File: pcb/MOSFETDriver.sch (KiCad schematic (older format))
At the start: 3 parts

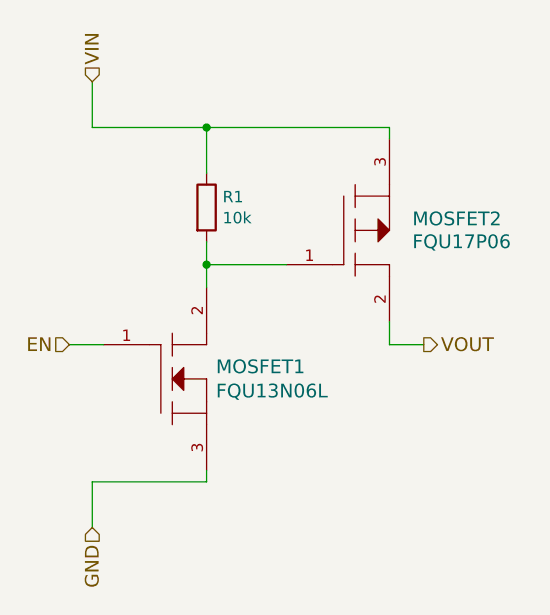
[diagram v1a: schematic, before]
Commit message: Display board connects via 6-wire connector
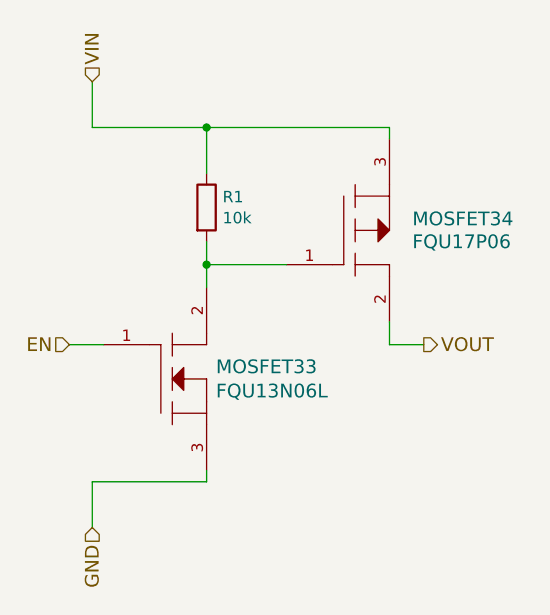
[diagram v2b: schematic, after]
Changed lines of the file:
@@
 $Descr A4 11693 8268
 encoding utf-8
-Sheet 2 19
+Sheet 19 19
 Title "Failinator"
 Date ""
@@
 AR Path="/56946533/56877F77" Ref="MOSFET45"  Part="1"
 AR Path="/5694653F/56877F77" Ref="MOSFET47"  Part="1"
-F 0 "MOSFET1" H 4991 4103 60  0000 L CNN
+AR Path="/5694859C/56932920/56877F77" Ref="MOSFET11"  Part="1"
+AR Path="/5694859C/56930DD4/56877F77" Ref="MOSFET7"  Part="1"
+AR Path="/5694859C/56931957/56877F77" Ref="MOSFET9"  Part="1"
+AR Path="/5694859C/56932F11/56877F77" Ref="MOSFET13"  Part="1"
+AR Path="/5694859C/5693327A/56877F77" Ref="MOSFET15"  Part="1"
+AR Path="/5694859C/56933823/56877F77" Ref="MOSFET17"  Part="1"
+AR Path="/5694859C/5693448C/56877F77" Ref="MOSFET19"  Part="1"
+AR Path="/5694859C/569464F7/56877F77" Ref="MOSFET21"  Part="1"
+AR Path="/5694859C/56946503/56877F77" Ref="MOSFET23"  Part="1"
+AR Path="/5694859C/5694650F/56877F77" Ref="MOSFET25"  Part="1"
+AR Path="/5694859C/5694651B/56877F77" Ref="MOSFET27"  Part="1"
+AR Path="/5694859C/56946527/56877F77" Ref="MOSFET29"  Part="1"
+AR Path="/5694859C/56946533/56877F77" Ref="MOSFET31"  Part="1"
+AR Path="/5694859C/5694653F/56877F77" Ref="MOSFET33"  Part="1"
+F 0 "MOSFET33" H 4991 4103 60  0000 L CNN
 F 1 "FQU13N06L" H 4991 3997 60  0000 L CNN
 F 2 "failinator:TO-251AA" H 4650 4050 60  0001 C CNN
@@
 AR Path="/56946533/56877F80" Ref="R16"  Part="1"
 AR Path="/5694653F/56877F80" Ref="R17"  Part="1"
+AR Path="/5694859C/56932920/56877F80" Ref="R1"  Part="1"
+AR Path="/5694859C/56930DD4/56877F80" Ref="R1"  Part="1"
+AR Path="/5694859C/56931957/56877F80" Ref="R1"  Part="1"
+AR Path="/5694859C/56932F11/56877F80" Ref="R1"  Part="1"
+AR Path="/5694859C/5693327A/56877F80" Ref="R1"  Part="1"
+AR Path="/5694859C/56933823/56877F80" Ref="R1"  Part="1"
+AR Path="/5694859C/5693448C/56877F80" Ref="R1"  Part="1"
+AR Path="/5694859C/569464F7/56877F80" Ref="R1"  Part="1"
+AR Path="/5694859C/56946503/56877F80" Ref="R1"  Part="1"
+AR Path="/5694859C/5694650F/56877F80" Ref="R1"  Part="1"
+AR Path="/5694859C/5694651B/56877F80" Ref="R1"  Part="1"
+AR Path="/5694859C/56946527/56877F80" Ref="R1"  Part="1"
+AR Path="/5694859C/56946533/56877F80" Ref="R1"  Part="1"
+AR Path="/5694859C/5694653F/56877F80" Ref="R1"  Part="1"
 F 0 "R1" H 5020 3346 50  0000 L CNN
 F 1 "10k" H 5020 3254 50  0000 L CNN
@@
 AR Path="/56946533/56877F87" Ref="MOSFET46"  Part="1"
 AR Path="/5694653F/56877F87" Ref="MOSFET48"  Part="1"
-F 0 "MOSFET2" H 5850 3450 60  0000 L CNN
+AR Path="/5694859C/56932920/56877F87" Ref="MOSFET12"  Part="1"
+AR Path="/5694859C/56930DD4/56877F87" Ref="MOSFET8"  Part="1"
+AR Path="/5694859C/56931957/56877F87" Ref="MOSFET10"  Part="1"
+AR Path="/5694859C/56932F11/56877F87" Ref="MOSFET14"  Part="1"
+AR Path="/5694859C/5693327A/56877F87" Ref="MOSFET16"  Part="1"
+AR Path="/5694859C/56933823/56877F87" Ref="MOSFET18"  Part="1"
+AR Path="/5694859C/5693448C/56877F87" Ref="MOSFET20"  Part="1"
+AR Path="/5694859C/569464F7/56877F87" Ref="MOSFET22"  Part="1"
+AR Path="/5694859C/56946503/56877F87" Ref="MOSFET24"  Part="1"
+AR Path="/5694859C/5694650F/56877F87" Ref="MOSFET26"  Part="1"
+AR Path="/5694859C/5694651B/56877F87" Ref="MOSFET28"  Part="1"
+AR Path="/5694859C/56946527/56877F87" Ref="MOSFET30"  Part="1"
+AR Path="/5694859C/56946533/56877F87" Ref="MOSFET32"  Part="1"
+AR Path="/5694859C/5694653F/56877F87" Ref="MOSFET34"  Part="1"
+F 0 "MOSFET34" H 5850 3450 60  0000 L CNN
 F 1 "FQU17P06" H 5850 3350 60  0000 L CNN
 F 2 "failinator:TO-251AA" H 5450 3400 60  0001 C CNN
